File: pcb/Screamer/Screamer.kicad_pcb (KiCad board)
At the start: 2 copper layers, 52 x 63 mm, 12 parts, among them J1 Conn_01x04, SW100 SW_DPDT_x2, SW101 SW_DPDT_x2

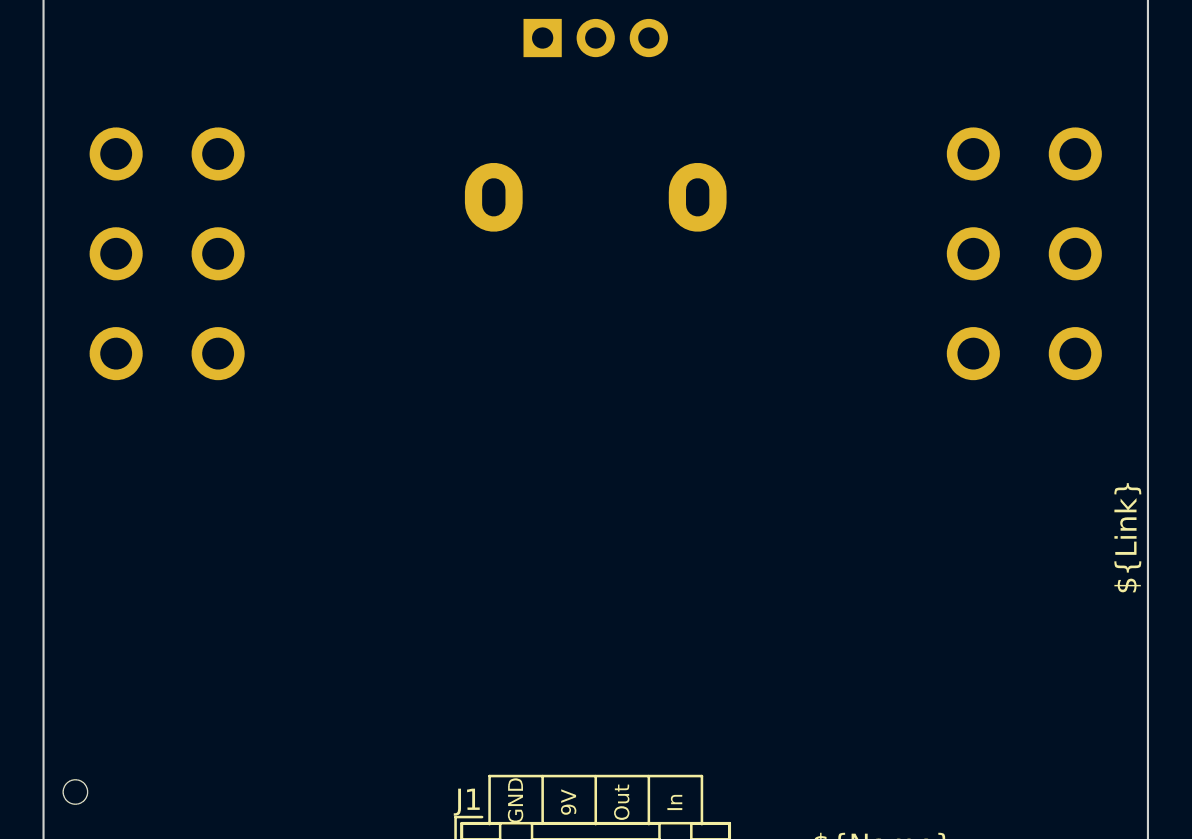
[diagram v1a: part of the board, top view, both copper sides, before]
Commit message: [Screamer] Update PCB with schematic updates
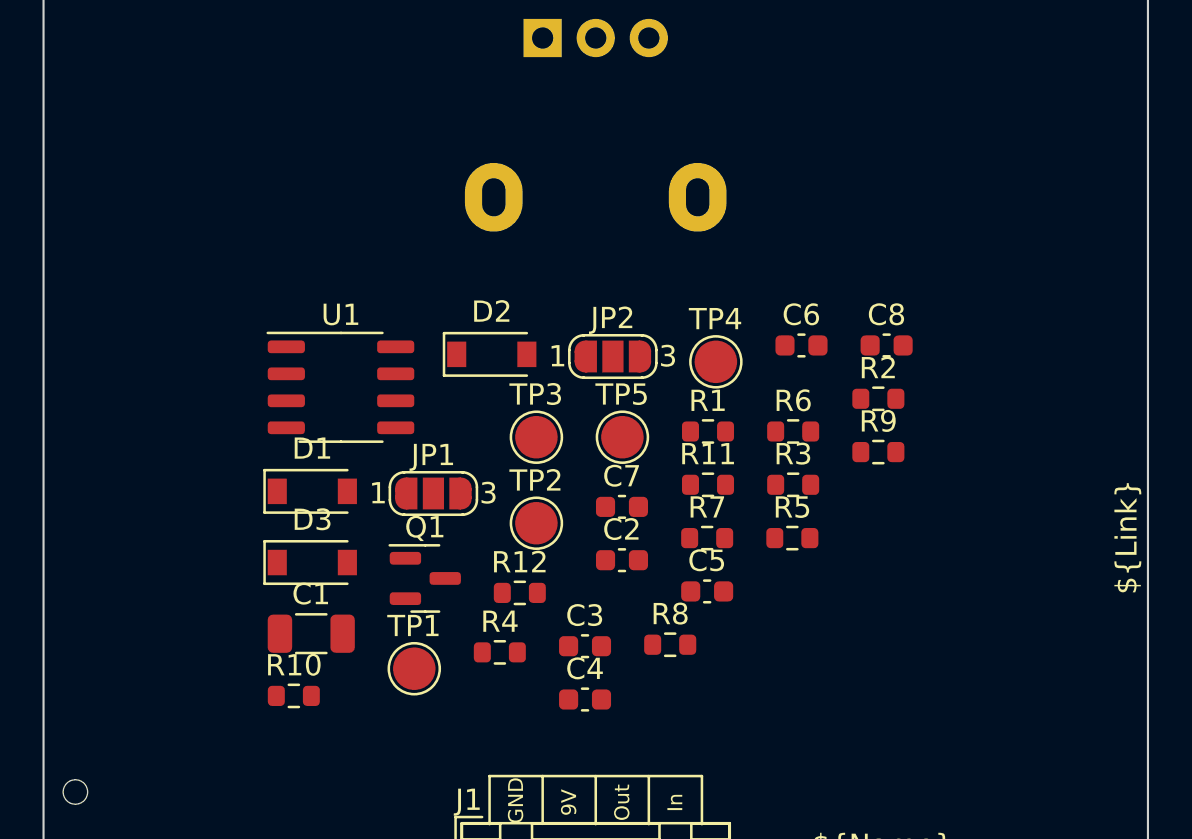
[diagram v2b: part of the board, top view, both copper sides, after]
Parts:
- removed SW100, SW101: SW_DPDT_x2, MeineBib:Switch_toggle_DPDT_Print
- added C1: 22uF, Capacitor_SMD:C_1206_3216Metric, F.Cu at (136.1, 115.6)
- added C2: 47n, Capacitor_SMD:C_0603_1608Metric, F.Cu at (150.7, 112.1)
- added C3: 1uF, Capacitor_SMD:C_0603_1608Metric, F.Cu at (149.0, 116.2)
- added C4: 47n, Capacitor_SMD:C_0603_1608Metric, F.Cu at (149.0, 118.7)
- added C5: 47pF, Capacitor_SMD:C_0603_1608Metric, F.Cu at (154.7, 113.6)
- added C6: 220nF, Capacitor_SMD:C_0603_1608Metric, F.Cu at (159.2, 102.0)
- added C7: 220nF, Capacitor_SMD:C_0603_1608Metric, F.Cu at (150.7, 109.6)
- added C8: 1uF, Capacitor_SMD:C_0603_1608Metric, F.Cu at (163.2, 102.0)
- added D1: 1N4148W, Diode_SMD:D_SOD-123, F.Cu at (136.2, 108.9)
- added D2: 1N4148W, Diode_SMD:D_SOD-123, F.Cu at (144.6, 102.4)
- added D3: 1N4148W, Diode_SMD:D_SOD-123, F.Cu at (136.2, 112.2)
- added JP1: SolderJumper, Jumper:SolderJumper-3_P1.3mm_Open_RoundedPad1.0x1.5mm_NumberLabels, F.Cu at (141.9, 109.0)
- added JP2: SolderJumper, Jumper:SolderJumper-3_P1.3mm_Open_RoundedPad1.0x1.5mm_NumberLabels, F.Cu at (150.3, 102.5)
- added Q1: BC846, Package_TO_SOT_SMD:SOT-23, F.Cu at (141.5, 113.0)
- added R1: 10K, Resistor_SMD:R_0603_1608Metric, F.Cu at (154.8, 106.1)
- added R10: 10K, Resistor_SMD:R_0603_1608Metric, F.Cu at (135.3, 118.5)
- added R11: 220R, Resistor_SMD:R_0603_1608Metric, F.Cu at (154.8, 108.6)
- added R12: 1K, Resistor_SMD:R_0603_1608Metric, F.Cu at (145.9, 113.7)
- added R2: 10K, Resistor_SMD:R_0603_1608Metric, F.Cu at (162.8, 104.5)
- added R3: 1K, Resistor_SMD:R_0603_1608Metric, F.Cu at (158.8, 108.6)
- added R4: 510K, Resistor_SMD:R_0603_1608Metric, F.Cu at (145.0, 116.5)
- added R5: 10K, Resistor_SMD:R_0603_1608Metric, F.Cu at (158.8, 111.1)
- added R6: 4K7, Resistor_SMD:R_0603_1608Metric, F.Cu at (158.8, 106.1)
- added R7: 10K, Resistor_SMD:R_0603_1608Metric, F.Cu at (154.7, 111.1)
- added R8: 51K, Resistor_SMD:R_0603_1608Metric, F.Cu at (153.0, 116.1)
- added R9: 1K, Resistor_SMD:R_0603_1608Metric, F.Cu at (162.8, 107.0)
- added TP1: TP, TestPoint:TestPoint_Pad_D2.0mm, F.Cu at (141.0, 117.2)
- added TP2: TP, TestPoint:TestPoint_Pad_D2.0mm, F.Cu at (146.7, 110.4)
- added TP3: TP, TestPoint:TestPoint_Pad_D2.0mm, F.Cu at (146.7, 106.3)
- added TP4: TP, TestPoint:TestPoint_Pad_D2.0mm, F.Cu at (155.2, 102.8)
- added TP5: TP, TestPoint:TestPoint_Pad_D2.0mm, F.Cu at (150.8, 106.3)
- added U1: RC4558, Package_SO:SO-8_3.9x4.9mm_P1.27mm, F.Cu at (137.5, 104.0)
- RV1: renamed from RV100; value 100K Lin -> 500K
- RV2: renamed from RV101; value 100K Lin -> 20k
- RV3: renamed from RV102; value 100K Lin -> 100K
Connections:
- RV1 pad 1: unconnected-(RV100-Pad1) -> Net-(RV1-Pad1)
- RV1 pad 2: unconnected-(RV100-Pad2) -> Net-(RV1-Pad2)
- RV1 pad 3: unconnected-(RV100-Pad3) -> Net-(RV1-Pad2)
- RV2 pad 1: unconnected-(RV101-Pad1) -> Net-(RV2-Pad1)
- RV2 pad 2: unconnected-(RV101-Pad2) -> Net-(RV2-Pad2)
- RV2 pad 3: unconnected-(RV101-Pad3) -> Net-(RV2-Pad3)
- RV3 pad 1: unconnected-(RV102-Pad1) -> GND
- RV3 pad 2: unconnected-(RV102-Pad2) -> Net-(RV3-Pad2)
- RV3 pad 3: unconnected-(RV102-Pad3) -> Upper_PCB_Output

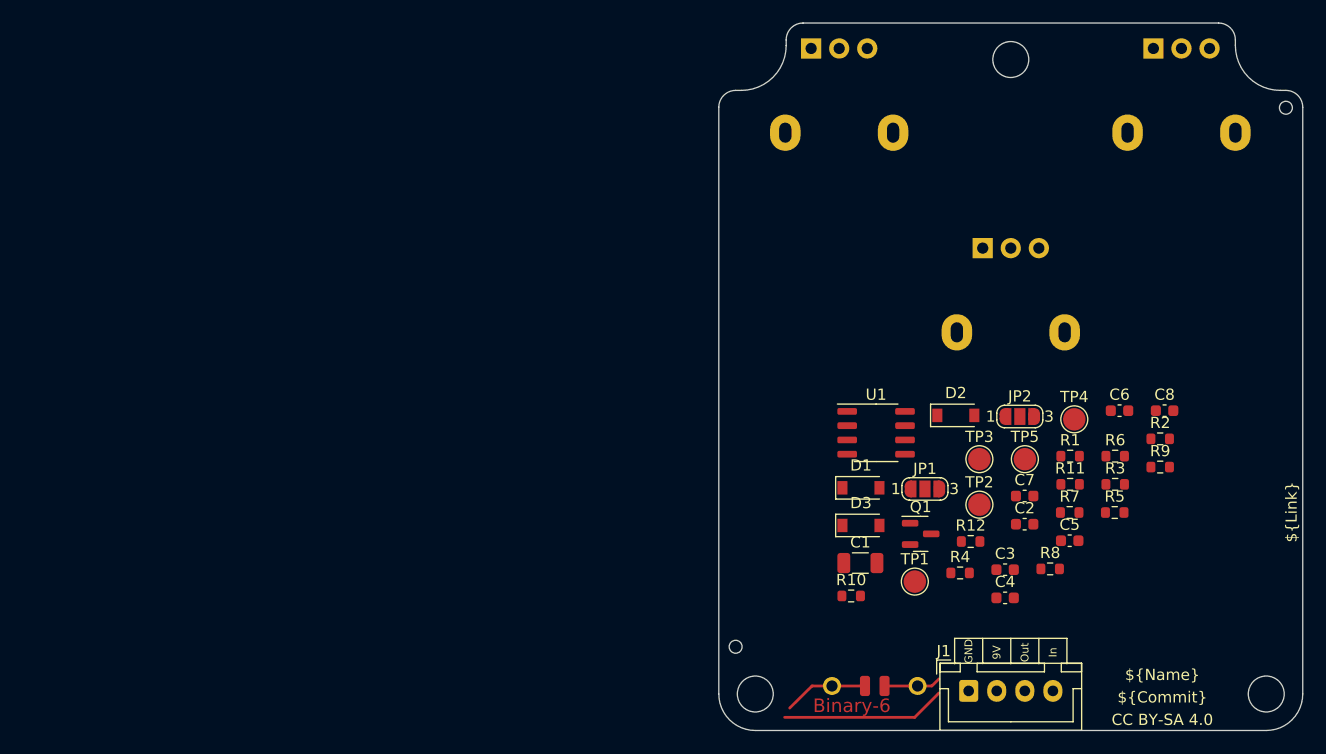
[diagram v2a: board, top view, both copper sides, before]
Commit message: [Screamer] Update diode footprint and start arranging stuff on PCB
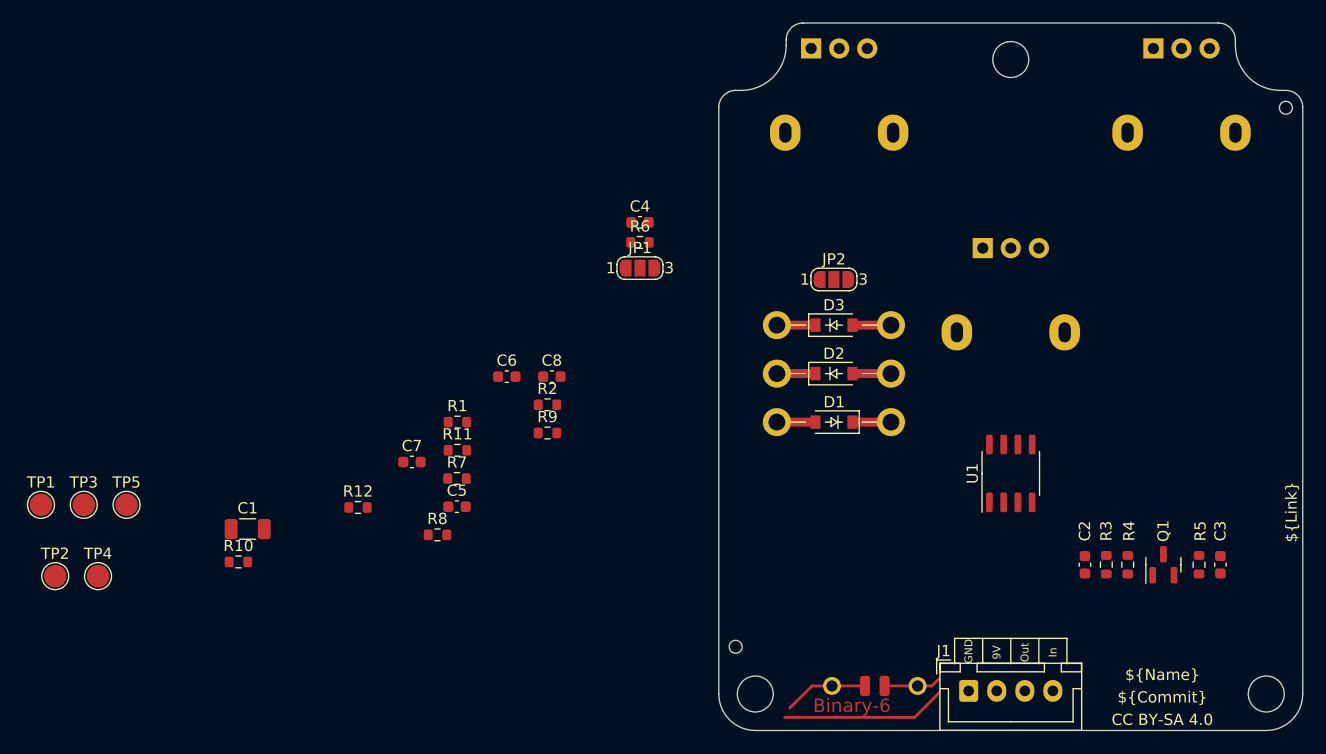
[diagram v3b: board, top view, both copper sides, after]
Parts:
- D1, D2, D3: footprint Diode_SMD:D_SOD-123 -> MeineBib:D_SOD-123+THT
- moved TP4 88.1 mm to (68.2, 116.8)
- moved TP2 82.5 mm to (64.4, 116.8)
- moved TP5 80.1 mm to (70.8, 110.4)
- moved TP3 79.9 mm to (67.0, 110.4)
- moved TP1 78.1 mm to (63.1, 110.4)
- moved C5 54.6 mm to (100.2, 110.6)
- moved C6 54.6 mm to (104.6, 99.0)
- moved R2 54.6 mm to (108.2, 101.5)
- moved R7 54.6 mm to (100.2, 108.1)
- moved R9 54.6 mm to (108.2, 104.0)
- moved C1 54.6 mm to (81.5, 112.6)
- moved C8 54.6 mm to (108.6, 99.0)
- moved R1 54.6 mm to (100.2, 103.0)
- moved R10 54.6 mm to (80.7, 115.5)
- moved R11 54.6 mm to (100.2, 105.5)
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
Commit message: [Screamer] Initially route Screamer PCB
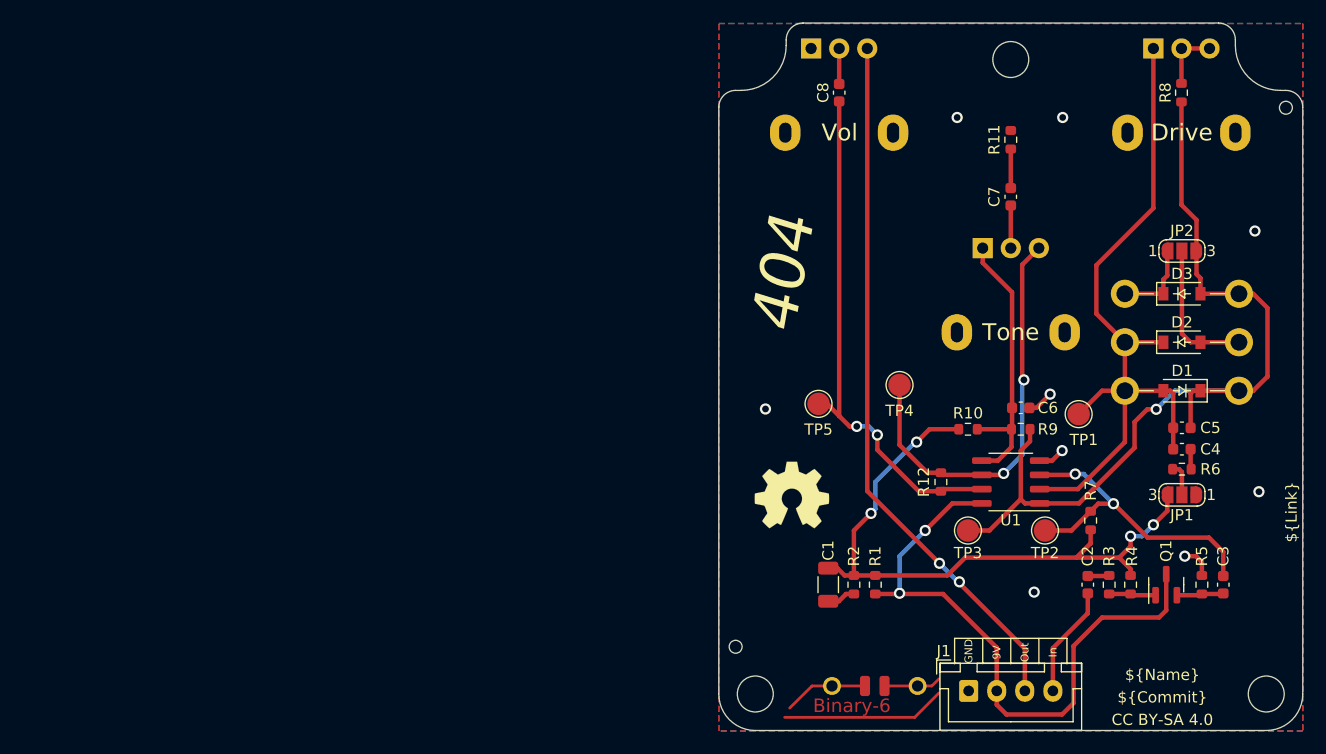
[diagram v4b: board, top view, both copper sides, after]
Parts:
- added REF**: OSHW-Symbol_6.7x6mm_SilkScreen, Symbol:OSHW-Symbol_6.7x6mm_SilkScreen, F.Cu at (130.0, 109.5)
- moved TP1 92.8 mm to (155.5, 102.3)
- moved TP2 88.2 mm to (152.5, 112.7), turned to 180 degrees
- moved TP3 78.8 mm to (145.7, 112.7), turned to 180 degrees
- moved R8 77.1 mm to (164.7, 73.7), turned to 90 degrees
- moved TP4 73.4 mm to (139.6, 99.7)
- moved R10 66.0 mm to (145.7, 103.7)
- moved C5 64.9 mm to (164.7, 103.5)
- moved TP5 62.3 mm to (132.4, 101.4)
- moved C7 58.3 mm to (149.5, 83.0), turned to 90 degrees
- moved R7 56.6 mm to (156.6, 111.8), turned to 90 degrees
- moved R11 56.5 mm to (149.5, 77.9), turned to 90 degrees
- moved C4 52.3 mm to (164.7, 105.5)
- moved JP1 52.3 mm to (164.7, 109.5), turned to 180 degrees
- moved R6 52.3 mm to (164.7, 107.2)
- moved R12 52.0 mm to (143.3, 108.4), turned to -90 degrees
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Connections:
- C1 pad 1: +9V -> +4V5
- JP1 pad 3: +9V -> +4V5
- R1 pad 2: +9V -> +4V5
- R10 pad 1: +9V -> +4V5
- R2 pad 1: +9V -> +4V5
- R4 pad 1: +9V -> +4V5
- R7 pad 1: +9V -> +4V5
- R8 pad 1: Net-(C4-Pad1) -> Net-(C5-Pad2)
- RV1 pad 1: Net-(R8-Pad2) -> Net-(C4-Pad1)
- RV1 pad 2: Net-(C5-Pad2) -> Net-(R8-Pad2)
- RV1 pad 3: Net-(C5-Pad2) -> Net-(R8-Pad2)
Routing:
- net Net-(C5-Pad2): track 0.00 -> 78.4 mm, vias 0 -> 1
- net Net-(C4-Pad1): track 0.00 -> 66.1 mm
- net Upper_PCB_Output: track 0.00 -> 63.1 mm, vias 0 -> 2
- net +4V5: track 0.00 -> 58.3 mm, vias 0 -> 4
- net +9V: track 0.00 -> 55.9 mm, vias 0 -> 2
- net Net-(C8-Pad1): track 0.00 -> 46.6 mm, vias 0 -> 2
- net Net-(R12-Pad1): track 0.00 -> 37.3 mm, vias 0 -> 2
- net Net-(C3-Pad2): track 0.00 -> 28.5 mm, vias 0 -> 2
- net Net-(C6-Pad1): track 0.00 -> 25.0 mm
- net Net-(D2-Pad2): track 0.00 -> 12.8 mm
- net GND: track 0.00 -> 10.2 mm, vias 0 -> 9
- net Upper_PCB_Input: track 0.00 -> 9.97 mm
- net Net-(D3-Pad1): track 0.00 -> 7.38 mm
- net Net-(R8-Pad2): track 0.00 -> 5.66 mm
- net Net-(C3-Pad1): track 0.07 -> 4.27 mm
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- added copper zone on B.Cu, net GND
- added copper zone on F.Cu, net GND
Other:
- board text added: "404"
- board text added: "Drive"
- board text added: "Tone"
- board text added: "Vol"

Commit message: [404] Update PCB
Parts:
- moved TP4 2.54 mm to (139.6, 102.3)
- moved TP5 0.95 mm to (132.0, 102.3)
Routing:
- net Net-(R12-Pad1): track 37.3 -> 34.7 mm
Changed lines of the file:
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@@
     (property "exclude_from_bom" "")
     (attr exclude_from_pos_files exclude_from_bom)
-    (fp_text reference "TP1" (at 0.4572 2.286) (layer "F.SilkS")
+    (fp_text reference "TP1" (at 0.0508 -2.0828) (layer "F.SilkS")
       (effects (font (size 1 1) (thickness 0.15)))
     )
@@
   )
   (footprint "TestPoint:TestPoint_Pad_D2.0mm" (layer "F.Cu")
-    (at 132.3804 101.4134)
+    (at 131.974 102.277)
     (descr "SMD pad as test Point, diameter 2.0mm")
     (tags "test point SMD pad")
@@
     (property "exclude_from_bom" "")
     (attr exclude_from_pos_files exclude_from_bom)
-    (fp_text reference "TP5" (at 0 2.286) (layer "F.SilkS")
+    (fp_text reference "TP5" (at 0 -2.032) (layer "F.SilkS")
       (effects (font (size 1 1) (thickness 0.15)))
     )
@@
   )
   (footprint "TestPoint:TestPoint_Pad_D2.0mm" (layer "F.Cu")
-    (at 139.594 99.737)
+    (at 139.594 102.277)
     (descr "SMD pad as test Point, diameter 2.0mm")
     (tags "test point SMD pad")
@@
     (property "exclude_from_bom" "")
     (attr exclude_from_pos_files exclude_from_bom)
-    (fp_text reference "TP4" (at 0 2.286) (layer "F.SilkS")
+    (fp_text reference "TP4" (at 0 -2.032) (layer "F.SilkS")
       (effects (font (size 1 1) (thickness 0.15)))
     )
@@
     (effects (font (size 1.5 1.5) (thickness 0.3)) (justify mirror))
   )
-  (gr_text "404" (at 129.25 89.795 80) (layer "F.SilkS")
+  (gr_text "404" (at 129.25 91.045 80) (layer "F.SilkS")
     (effects (font (size 4 4) (thickness 1) italic))
   )
@@
     (effects (font (size 0.7 0.7) (thickness 0.13)))
   )
-  (gr_text "404" (at 129.25 89.795 80) (layer "F.Mask")
+  (gr_text "404" (at 129.25 91.045 80) (layer "F.Mask")
     (effects (font (size 4 4) (thickness 0.6) italic))
   )
@@
   (via (at 154.072 105.579) (size 1) (drill 0.6) (layers "F.Cu" "B.Cu") (net 2))
   (via (at 151.5828 118.1774) (size 1) (drill 0.6) (layers "F.Cu" "B.Cu") (free) (net 2))
-  (via (at 144.7248 75.9118) (size 1) (drill 0.6) (layers "F.Cu" "B.Cu") (free) (net 2))
+  (via (at 145 75.9118) (size 1) (drill 0.6) (layers "F.Cu" "B.Cu") (free) (net 2))
   (via (at 171.2424 86.021) (size 1) (drill 0.6) (layers "F.Cu" "B.Cu") (free) (net 2))
   (via (at 164.994 114.977) (size 1) (drill 0.6) (layers "F.Cu" "B.Cu") (net 2))
@@
   (segment (start 149.5 82.198) (end 149.5 78.718) (width 0.4) (layer "F.Cu") (net 11))
   (segment (start 141.308 109.198) (end 143.277 109.198) (width 0.4) (layer "F.Cu") (net 12))
-  (segment (start 133.1424 101.4134) (end 134.22 102.491) (width 0.4) (layer "F.Cu") (net 12))
+  (segment (start 131.974 102.277) (end 134.006 102.277) (width 0.4) (layer "F.Cu") (net 12))
   (segment (start 137.6195 104.182) (end 137.6195 105.5095) (width 0.4) (layer "F.Cu") (net 12))
   (segment (start 134.22 102.491) (end 135.149 103.42) (width 0.4) (layer "F.Cu") (net 12))
@@
   (segment (start 135.149 103.42) (end 135.784 103.42) (width 0.4) (layer "F.Cu") (net 12))
   (segment (start 143.467 109.008) (end 143.277 109.198) (width 0.4) (layer "F.Cu") (net 12))
-  (segment (start 132.3804 101.4134) (end 133.1424 101.4134) (width 0.4) (layer "F.Cu") (net 12))
+  (segment (start 134.006 102.277) (end 134.22 102.491) (width 0.4) (layer "F.Cu") (net 12))
   (via (at 137.6195 104.182) (size 1) (drill 0.6) (layers "F.Cu" "B.Cu") (net 12))
   (via (at 135.784 103.42) (size 1) (drill 0.6) (layers "F.Cu" "B.Cu") (net 12))
@@
   (segment (start 164.7 69.765) (end 167.2 69.765) (width 0.4) (layer "F.Cu") (net 20))
   (segment (start 164.7 69.765) (end 164.651663 69.765) (width 0.4) (layer "F.Cu") (net 20))
-  (segment (start 139.594 105.071) (end 139.594 99.737) (width 0.4) (layer "F.Cu") (net 21))
   (segment (start 146.925 107.738) (end 143.467 107.738) (width 0.4) (layer "F.Cu") (net 21))
   (segment (start 148.865 107.611) (end 148.738 107.738) (width 0.4) (layer "F.Cu") (net 21))
   (segment (start 148.738 107.738) (end 146.925 107.738) (width 0.4) (layer "F.Cu") (net 21))
-  (segment (start 143.277 107.548) (end 142.071 107.548) (width 0.4) (layer "F.Cu") (net 21))
   (segment (start 150.516 89.029) (end 152 87.545) (width 0.4) (layer "F.Cu") (net 21))
+  (segment (start 142.071 107.548) (end 139.594 105.071) (width 0.4) (layer "F.Cu") (net 21))
   (segment (start 150.6684 99.2798) (end 150.516 99.1274) (width 0.4) (layer "F.Cu") (net 21))
   (segment (start 143.467 107.738) (end 143.277 107.548) (width 0.4) (layer "F.Cu") (net 21))
-  (segment (start 142.071 107.548) (end 139.594 105.071) (width 0.4) (layer "F.Cu") (net 21))
+  (segment (start 139.594 105.071) (end 139.594 102.277) (width 0.4) (layer "F.Cu") (net 21))
+  (segment (start 143.277 107.548) (end 142.071 107.548) (width 0.4) (layer "F.Cu") (net 21))
   (segment (start 150.516 99.1274) (end 150.516 89.029) (width 0.4) (layer "F.Cu") (net 21))
   (via (at 148.865 107.611) (size 1) (drill 0.6) (layers "F.Cu" "B.Cu") (net 21))
